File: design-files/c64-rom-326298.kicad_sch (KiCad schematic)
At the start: 16 parts, among them J1 Conn_01x12_Pin, J2 Conn_01x12_Pin, J3 Conn_01x02_Pin, J4 Conn_01x04_Pin, J5 Conn_01x12_Pin, SW101 SW_DIP_x02, SW102 SW_DIP_x02, SW103 SW_DIP_x02, U101 SST39SF010, U102 GAL22V10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

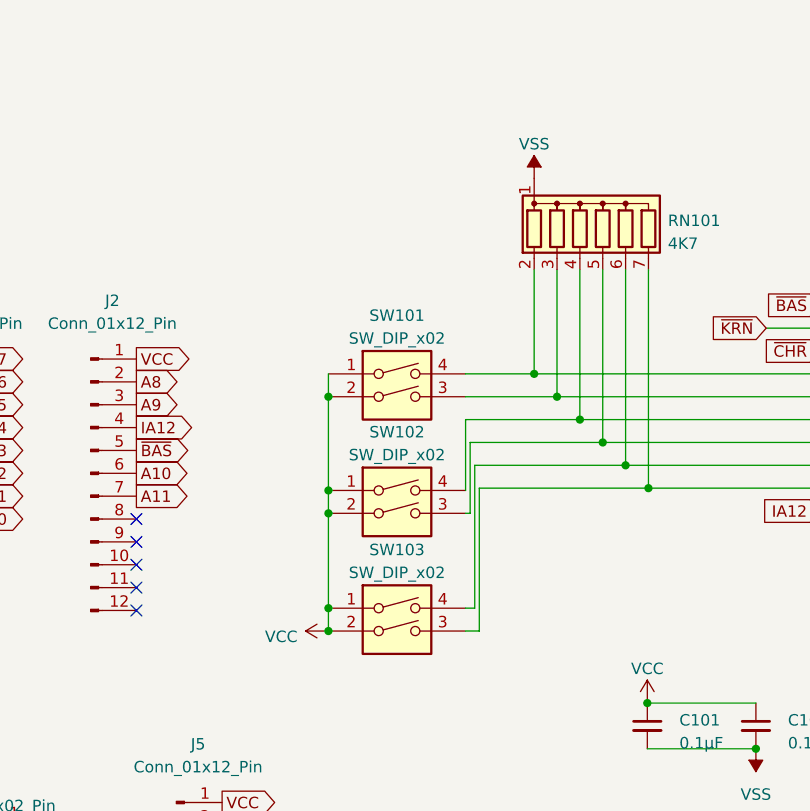
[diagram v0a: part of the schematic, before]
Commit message: Re-arrange the inputs to the GAL and make them active-low.
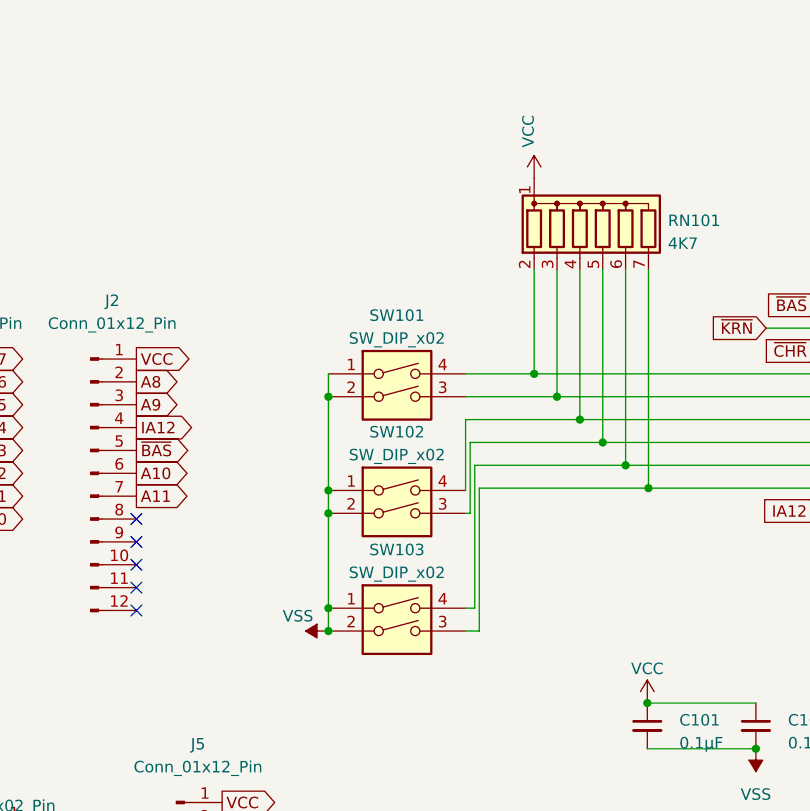
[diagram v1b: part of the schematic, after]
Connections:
- net VCC: now also RN101.1 (common); no longer SW101.1, SW101.2, SW102.1, SW102.2, SW103.1, SW103.2
- net VSS: now also SW101.1, SW101.2, SW102.1, SW102.2, SW103.1, SW103.2; no longer RN101.1 (common)
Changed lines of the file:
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@@
   (junction (at 162.941 65.024) (diameter 0) (color 0 0 0 0)
   )
+  (junction (at 132.461 85.979) (diameter 0) (color 0 0 0 0)
+  )
   (junction (at 132.461 72.898) (diameter 0) (color 0 0 0 0)
   )
@@
   )
   (junction (at 157.861 59.944) (diameter 0) (color 0 0 0 0)
-  )
-  (junction (at 132.461 85.979) (diameter 0) (color 0 0 0 0)
   )
   (no_connect (at 187.071 77.724))
@@
     )
   )
-  (symbol (lib_id "power:VSS") (at 155.321 35.687 0) (unit 1)
-    (in_bom yes) (on_board yes) (dnp no) (fields_autoplaced)
-    (property "Reference" "#PWR0107" (at 155.321 39.497 0)
-      (effects (font (size 1.27 1.27)) hide)
-    )
-    (property "Value" "VSS" (at 155.321 31.877 0)
-      (effects (font (size 1.27 1.27)))
-    )
-    (property "Footprint" "" (at 155.321 35.687 0)
-      (effects (font (size 1.27 1.27)) hide)
-    )
-    (property "Datasheet" "" (at 155.321 35.687 0)
+  (symbol (lib_id "power:VSS") (at 132.461 85.979 90) (unit 1)
+    (in_bom yes) (on_board yes) (dnp no)
+    (property "Reference" "#PWR0107" (at 136.271 85.979 0)
+      (effects (font (size 1.27 1.27)) hide)
+    )
+    (property "Value" "VSS" (at 127.381 84.328 90)
+      (effects (font (size 1.27 1.27)) (justify right))
+    )
+    (property "Footprint" "" (at 132.461 85.979 0)
+      (effects (font (size 1.27 1.27)) hide)
+    )
+    (property "Datasheet" "" (at 132.461 85.979 0)
       (effects (font (size 1.27 1.27)) hide)
     )
@@
     )
   )
-  (symbol (lib_id "power:VCC") (at 132.461 85.979 90) (unit 1)
-    (in_bom yes) (on_board yes) (dnp no) (fields_autoplaced)
-    (property "Reference" "#PWR0108" (at 136.271 85.979 0)
-      (effects (font (size 1.27 1.27)) hide)
-    )
-    (property "Value" "VCC" (at 129.032 86.614 90)
+  (symbol (lib_id "power:VCC") (at 155.321 35.687 0) (unit 1)
+    (in_bom yes) (on_board yes) (dnp no)
+    (property "Reference" "#PWR0108" (at 155.321 39.497 0)
+      (effects (font (size 1.27 1.27)) hide)
+    )
+    (property "Value" "VCC" (at 154.686 32.258 90)
       (effects (font (size 1.27 1.27)) (justify left))
     )
-    (property "Footprint" "" (at 132.461 85.979 0)
-      (effects (font (size 1.27 1.27)) hide)
-    )
-    (property "Datasheet" "" (at 132.461 85.979 0)
-      (effects (font (size 1.27 1.27)) hide)
-    )
+    (property "Footprint" "" (at 155.321 35.687 0)
+      (effects (font (size 1.27 1.27)) hide)
+    )
+    (property "Datasheet" "" (at 155.321 35.687 0)
+      (effects (font (size 1.27 1.27)) hide)
+    )

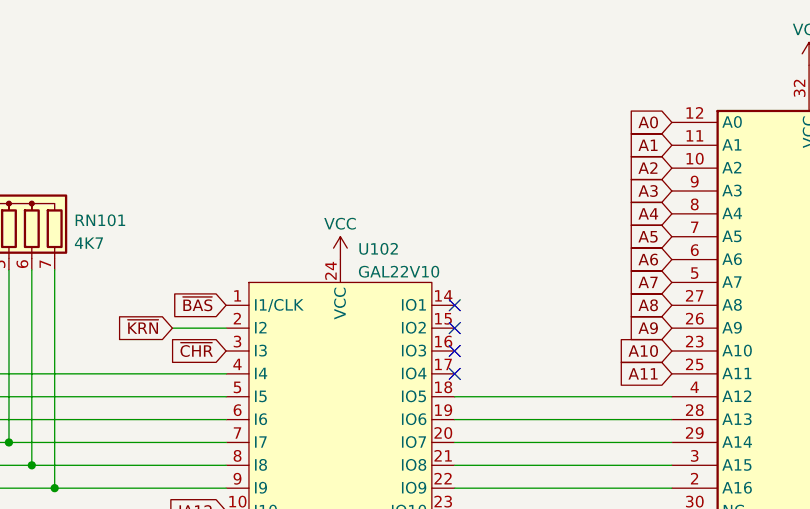
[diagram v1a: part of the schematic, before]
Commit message: Re-route the boards after fixing the pin spacing.
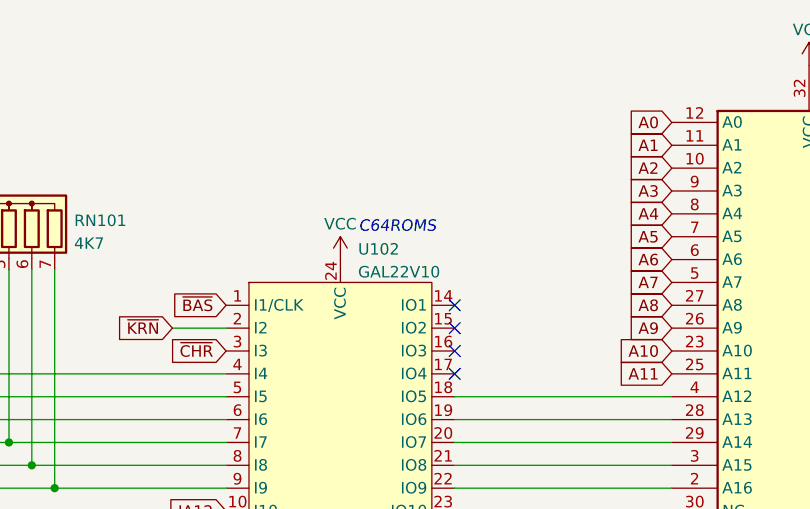
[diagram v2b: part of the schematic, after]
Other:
- note added: "C64ROMS"
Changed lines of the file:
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@@
   (title_block
     (title "Commodore 64 326298 ROM Replacer / Selector")
-    (date "2023-10-28")
+    (date "2023-12-14")
     (rev "1.0")
     (company "Copyright (c) 2023 Jason R. Thorpe. See LICENSE.")
@@
     (stroke (width 0) (type default))
   )
+  (text "C64ROMS" (at 201.803 41.91 0)
+    (effects (font (size 1.27 1.27) italic) (justify left bottom))
+  )
   (global_label "A8" (shape input) (at 38.862 168.529 180) (fields_autoplaced)
